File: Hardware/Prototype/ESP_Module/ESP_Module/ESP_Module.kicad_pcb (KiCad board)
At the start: 4 copper layers, 18.5 x 37.5 mm, 14 parts, among them J1 48037-0001, SW1 SW_SPST, SW2 SW_SPST, U1 AMS1117-3.3, U2 ESP32-S3-MINI-1-N8

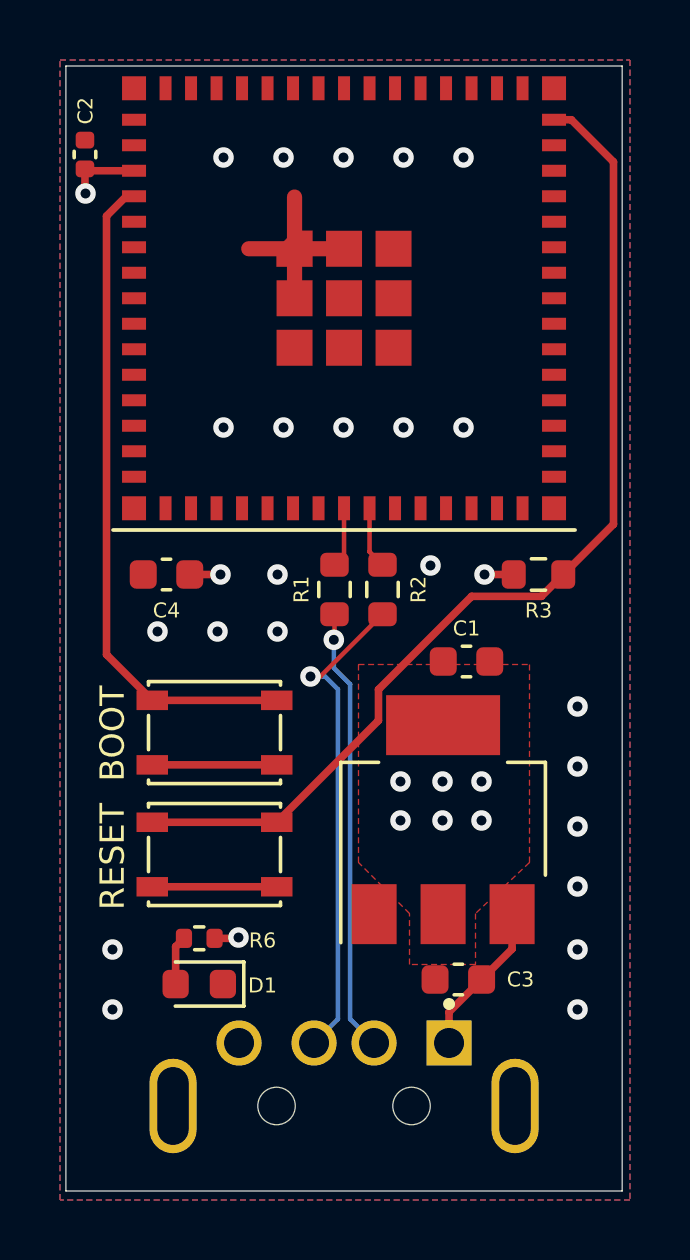
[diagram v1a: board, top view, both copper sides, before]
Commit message: Added ESP SoC PCB Files
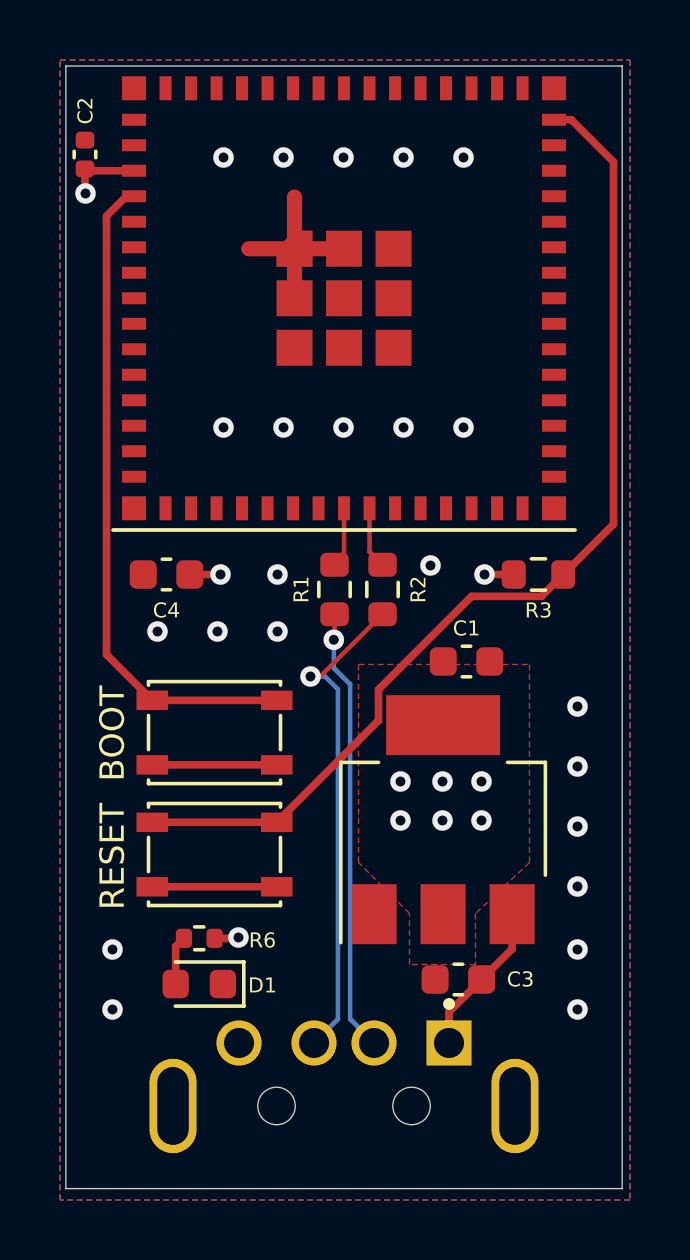
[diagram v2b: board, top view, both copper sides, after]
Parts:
- added G***: LOGO, LOGO, B.Cu at (157.2, 76.3)
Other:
- board size 18.5 x 37.5 mm -> 18.5 x 37.4 mm
